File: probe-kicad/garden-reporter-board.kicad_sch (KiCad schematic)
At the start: 21 parts, among them J1 70543-0106, J2 Conn_01x02, J3 70543-0002, J4 70543-0002, J5 70543-0002, Q1 TN0702N3-G, U1 MCP1700-3302E_TO92, U2 MCP1700-3302E_TO92

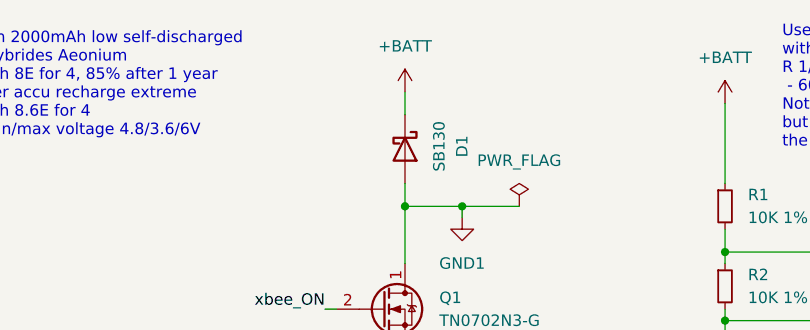
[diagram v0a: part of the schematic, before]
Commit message: Fix bad flyback diode connection, move xbee edge drawing to fron silkscreen
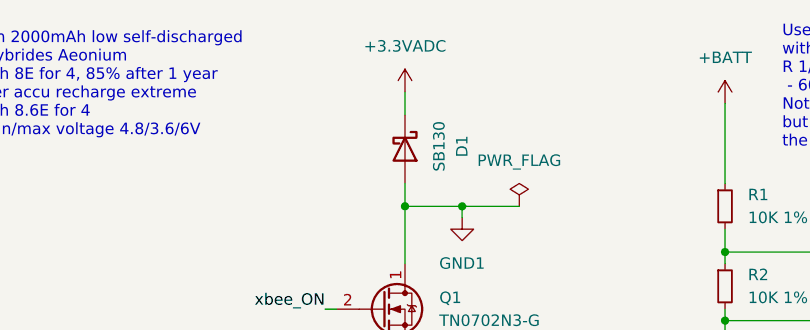
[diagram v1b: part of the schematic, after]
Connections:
- net +3.3VADC: now also D1.1 (K)
- net +BATT: no longer D1.1 (K)
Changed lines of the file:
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@@
     (pin "3")
+  )
+  (symbol (lib_id "power:+3.3VADC") (at 95.25 22.86 0) (unit 1)
+    (in_bom yes) (on_board yes)
+    (property "Reference" "#PWR?" (id 0) (at 99.06 24.13 0)
+      (effects (font (size 1.27 1.27)) hide)
+    )
+    (property "Value" "+3.3VADC" (id 1) (at 95.25 17.78 0))
+    (property "Footprint" "" (id 2) (at 95.25 22.86 0)
+      (effects (font (size 1.27 1.27)) hide)
+    )
+    (property "Datasheet" "" (id 3) (at 95.25 22.86 0)
+      (effects (font (size 1.27 1.27)) hide)
+    )
+    (pin "1")
   )
   (symbol (lib_id "power:+3.3VADC") (at 220.98 26.67 0) (unit 1)
@@
     (pin "3")
   )
-  (symbol (lib_id "power:+BATT") (at 95.25 22.86 0) (unit 1)
-    (in_bom yes) (on_board yes) (fields_autoplaced)
-    (property "Reference" "#PWR011" (id 0) (at 95.25 26.67 0)
-      (effects (font (size 1.27 1.27)) hide)
-    )
-    (property "Value" "+BATT" (id 1) (at 95.25 17.78 0))
-    (property "Footprint" "" (id 2) (at 95.25 22.86 0)
-      (effects (font (size 1.27 1.27)) hide)
-    )
-    (property "Datasheet" "" (id 3) (at 95.25 22.86 0)
-      (effects (font (size 1.27 1.27)) hide)
-    )
-    (pin "1")
-  )
   (symbol (lib_id "power:-BATT") (at 26.67 46.99 180) (unit 1)
     (in_bom yes) (on_board yes) (fields_autoplaced)
@@
       (reference "#PWR010") (unit 1) (value "GND") (footprint "")
     )
-    (path "/f3a0231f-7ba3-48dc-9d0b-ed2692750d42"
-      (reference "#PWR011") (unit 1) (value "+BATT") (footprint "")
-    )
     (path "/8838c3d2-eb16-4de4-b06c-9de5f335cde8"
       (reference "#PWR012") (unit 1) (value "-BATT") (footprint "")
@@
       (reference "#PWR024") (unit 1) (value "GND1") (footprint "")
     )
+    (path "/b06b4308-ed5c-4cf7-9c6f-ddf10a56cb44"
+      (reference "#PWR?") (unit 1) (value "+3.3VADC") (footprint "")
+    )
     (path "/d73750cc-a6d9-4a7f-87a2-5ca595640ba3"
